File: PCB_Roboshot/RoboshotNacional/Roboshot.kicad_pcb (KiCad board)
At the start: 2 copper layers, 63.3 x 86 mm, 35 parts, among them J1 Conn_01x08, Q1_LIGHT1 BC546, SW1 SW_Push_Dual_x2, U1 7840-0000PR, U2 H

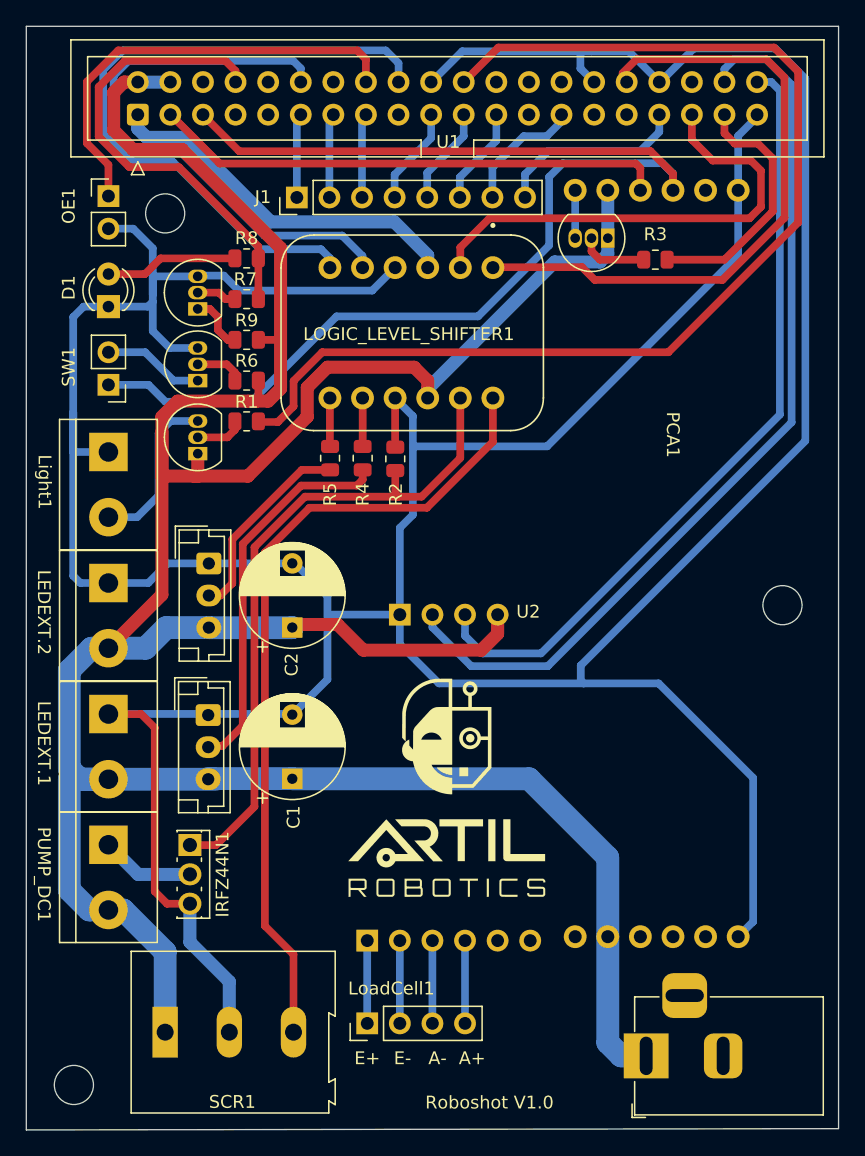
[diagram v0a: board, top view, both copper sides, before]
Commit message: Cambios en placa para china y para artesanal
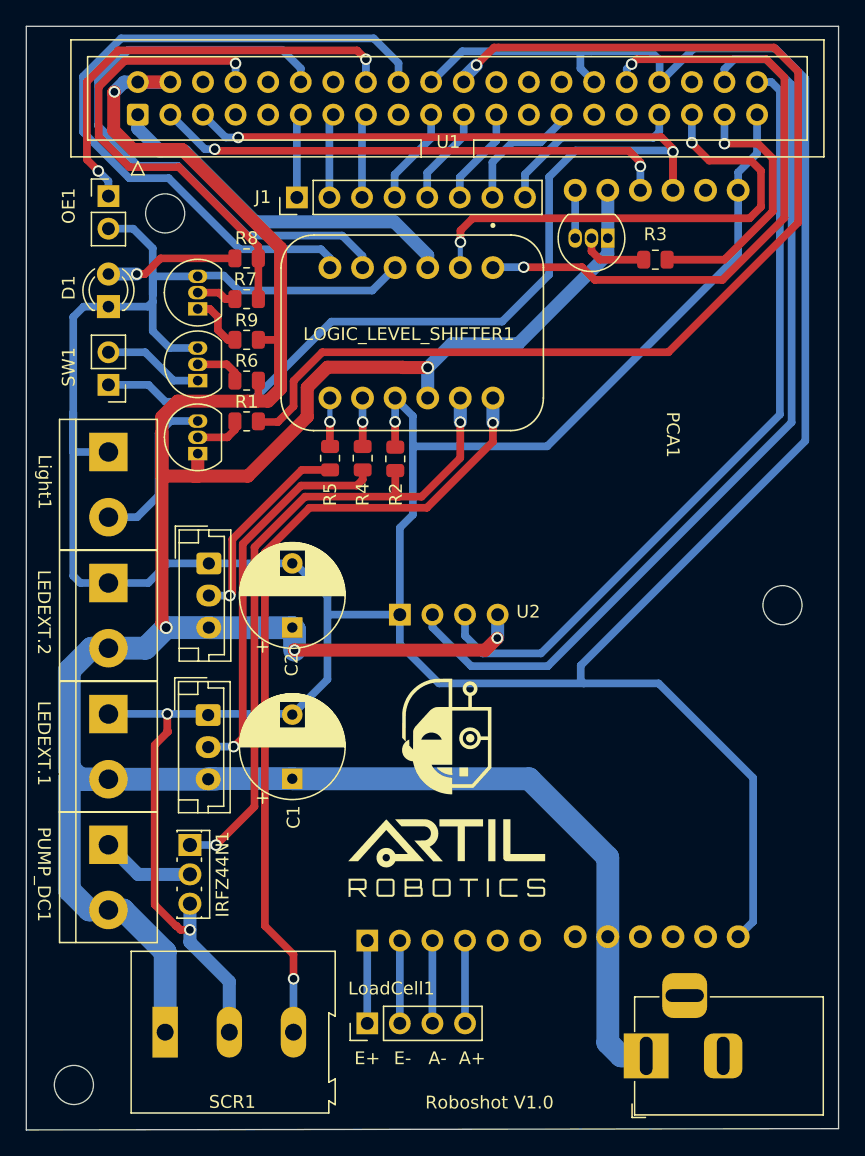
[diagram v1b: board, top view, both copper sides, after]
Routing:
- net /GPIO3(SCL1): track 96.8 -> 101.2 mm, vias 0 -> 2
- net /GPIO24(GEN5): track 52.8 -> 56.5 mm
- net /GPIO18(GEN1)(PWM0): track 44.8 -> 47.7 mm
- net /GPIO19(SPI1_MISO): track 37.5 -> 38.4 mm, vias 0 -> 2
- net Net-(LEDSIGN1-Pad2): track 29.7 -> 30.3 mm, vias 0 -> 1
- net /GPIO26: track 19.9 -> 20.4 mm, vias 0 -> 1
- net /GPIO14(TXD0): track 36.7 -> 37.1 mm, vias 0 -> 1
- net /HV3: track 3.37 -> 3.78 mm, vias 0 -> 1
- net +5V: track 265.1 -> 264.7 mm, vias 0 -> 5
- net /GPIO2(SDA1): track 40.0 -> 40.3 mm, vias 0 -> 2
- net /HV2: track 52.4 -> 52.2 mm, vias 0 -> 2
- net /GPIO25(GEN6): track 88.9 -> 89.1 mm, vias 0 -> 1
- net GND: track 354.7 -> 354.9 mm, vias 0 -> 3
- net /GPIO12(PWM0): track 50.4 -> 50.3 mm, vias 0 -> 2
- net /HV4: vias 0 -> 2
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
